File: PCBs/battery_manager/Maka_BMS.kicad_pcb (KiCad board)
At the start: 2 copper layers, 39 x 35.2 mm, 83 parts, among them J8 T1M-10-F-SH-L-K, J9 Molex 087340-1424, Q1 FDC645N, Q2 FDC645N, Q3 FDC645N, Q4 Si3483CDV, Q5 Si3483CDV, Q6 FDC645N, U1 AP63205, U2 TPS70933DBV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

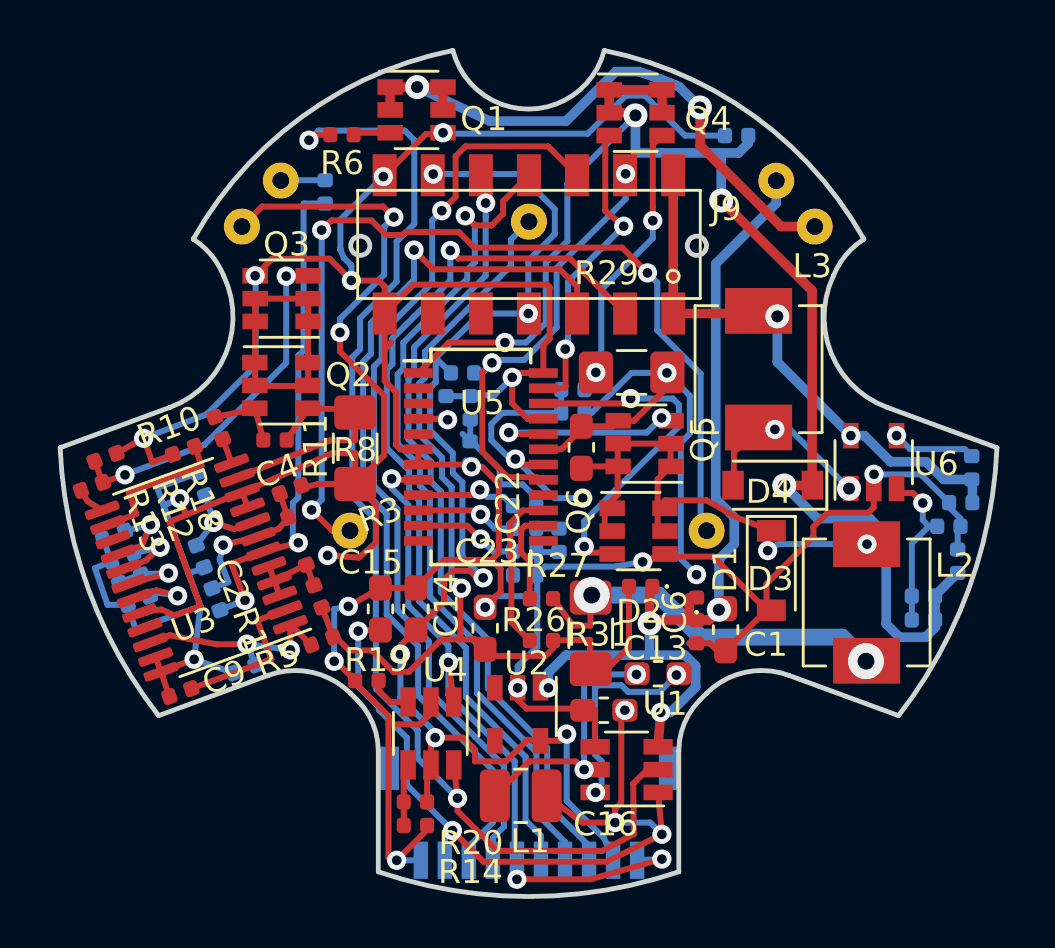
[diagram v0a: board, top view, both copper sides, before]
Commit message: Icreased trace thickness and rerouted higher freq and power paths in the battery management board
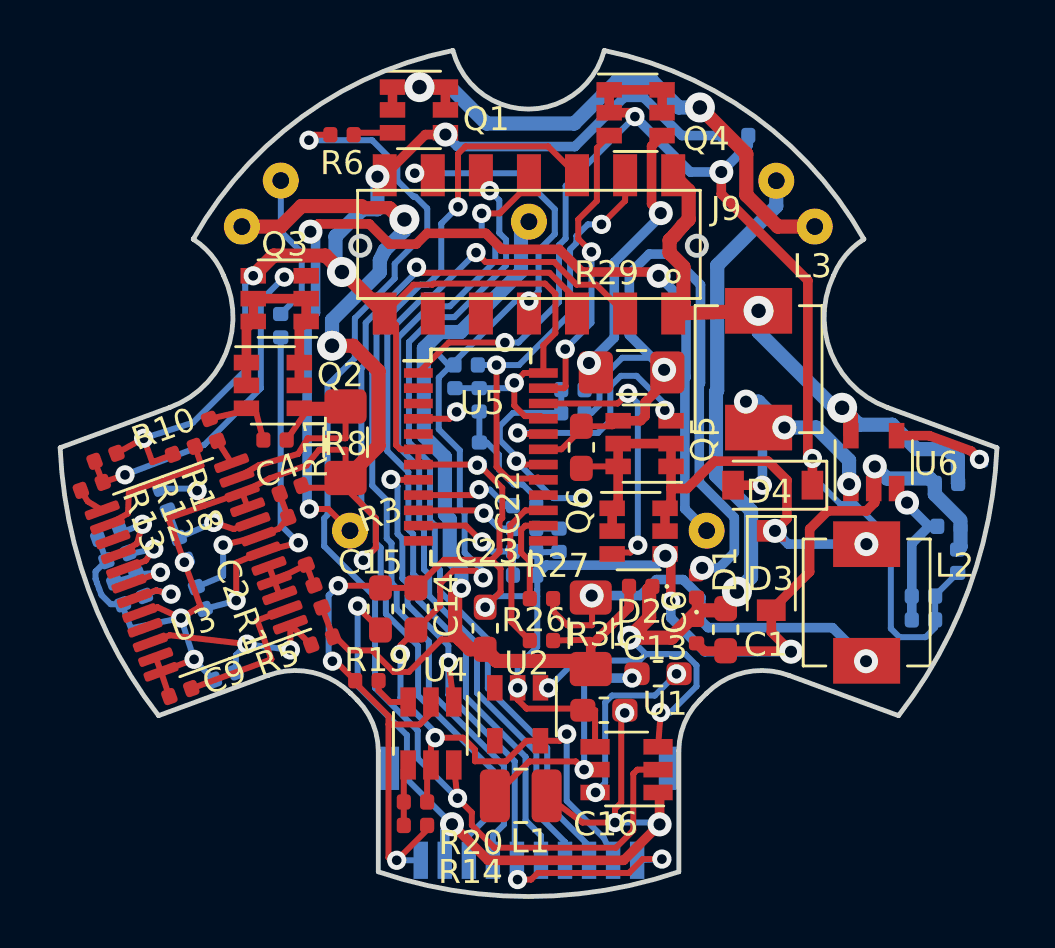
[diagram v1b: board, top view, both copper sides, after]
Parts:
- C24: value 1.75uF -> 0.15uF
- moved R2 5.86 mm to (142.1, 97.4)
- moved C5 1.67 mm to (137.2, 104.6)
- moved C7 1.00 mm to (169.8, 103.9)
- moved C8 0.86 mm to (139.8, 111.9)
- moved R4 0.80 mm to (138.0, 106.7)
- moved C3 0.65 mm to (138.7, 108.7)
- moved R24 0.50 mm to (149.3, 100.5)
- moved TH2 0.50 mm to (150.3, 100.5)
- moved R8 0.47 mm to (144.8, 102.2)
- moved C17 0.39 mm to (150.3, 102.7)
- moved R23 0.36 mm to (149.8, 99.0)
- moved Q2 0.35 mm to (141.8, 99.8)
- moved R21 0.34 mm to (170.7, 103.0), turned to 180 degrees
- moved R10 0.24 mm to (139.3, 101.7)
- moved R16 0.20 mm to (135.3, 107.0)
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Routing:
- net VCC: track 20.2 -> 33.9 mm
- net -BATT: track 69.6 -> 58.8 mm, vias 5 -> 7
- net Net-(C2-Pad1): track 21.0 -> 14.5 mm
- net Net-(7.4-Pad1): track 1.85 -> 6.29 mm
- net Net-(D4-Pad2): track 6.90 -> 11.3 mm, vias 2 -> 4
- net Earth: track 145.4 -> 149.4 mm, vias 14 -> 16
- net Net-(Q6-Pad2): track 14.7 -> 11.3 mm
- net +15V: track 58.7 -> 56.1 mm
- net Net-(12V_OUT1-Pad1): track 37.9 -> 40.5 mm
- net Net-(Q5-Pad2): track 8.07 -> 10.3 mm
- net Net-(Q2-Pad1): track 11.7 -> 9.67 mm
- net +12V: track 22.3 -> 24.0 mm
- net Net-(C22-Pad1): track 21.6 -> 23.2 mm
- net +BATT: track 39.6 -> 41.0 mm
- net Net-(L2-Pad2): track 15.9 -> 17.3 mm
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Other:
- net class 2.2A_Power added: clearance 0.2, trace_width 0.59, via_dia 1.25, via_drill 0.6
- net class 2.5A_Power removed
- board text added: "Maka"
- board text added: "Niu BMS"
- board text added: "rev.0"

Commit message: updates to battery managemennt wayfinder boards, and makaniu hall sensor ring and BMS
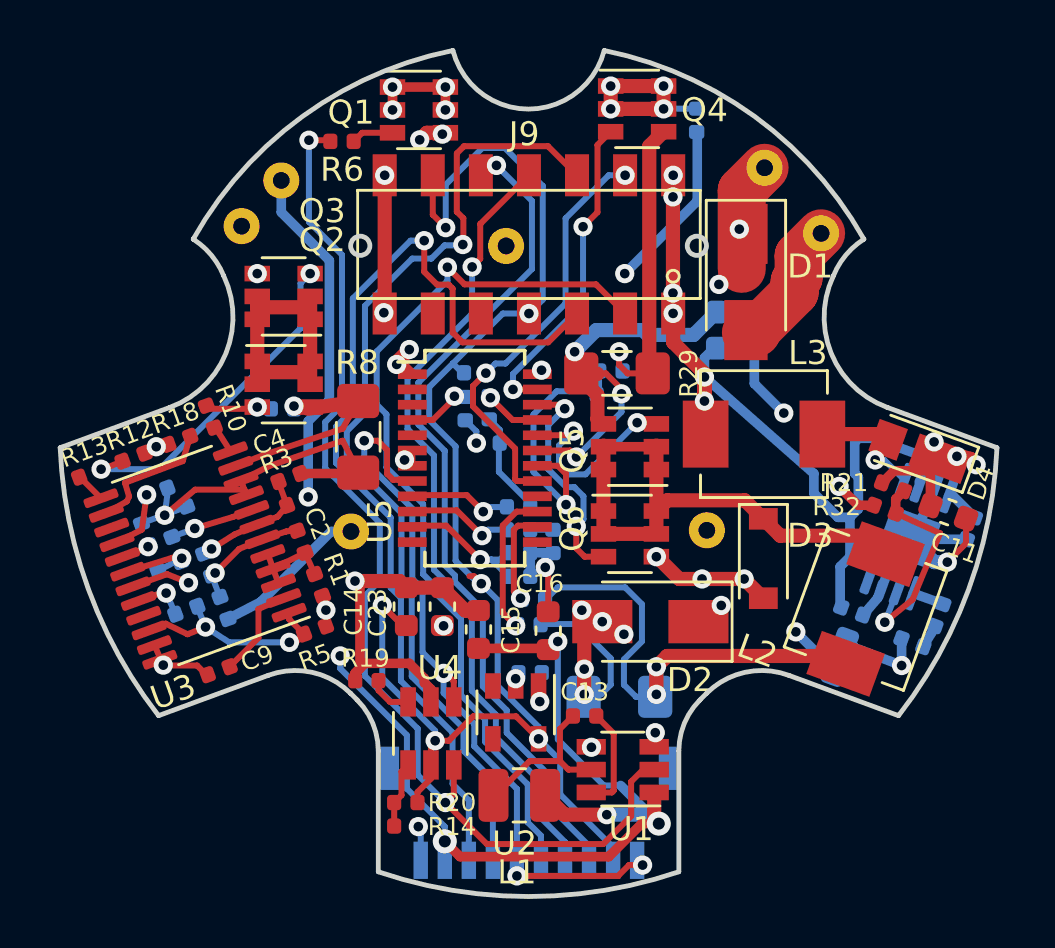
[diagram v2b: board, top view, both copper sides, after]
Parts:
- removed 3.4_2: 3.4+, Custom:TruHole_Batter_Contact_Pad_with_9mm_clear
- removed 7.4: 7.4, TestPoint:TestPoint_THTPad_D1.5mm_Drill0.7mm
- removed C24: 0.15uF, Capacitor_SMD:C_0402_1005Metric
- removed R33: 150K, Resistor_SMD:R_0402_1005Metric
- added 7.4_1: 7.4, Custom:TruHole_Batter_Contact_Pad_with_9mm_clear, B.Cu at (145.0, 105.9)
- added 7.4_2: 7.4, Custom:TruHole_Batter_Contact_Pad_with_9mm_clear, B.Cu at (159.8, 105.9)
- added C11: 10uF, Capacitor_SMD:C_0603_1608Metric, F.Cu at (169.8, 105.1)
- added C12: 15nF, Capacitor_SMD:C_0402_1005Metric, B.Cu at (170.8, 105.8)
- added R7: 100K, Resistor_SMD:R_0402_1005Metric, B.Cu at (165.8, 109.2)
- added R9: 15K, Resistor_SMD:R_0402_1005Metric, B.Cu at (168.3, 110.5)
- 0.0: renamed from 0_1; value 0 -> 0.0; footprint TestPoint:TestPoint_THTPad_D1.5mm_Drill0.7mm -> Custom:TruHole_Batter_Contact_Pad_with_9mm_clear
- 11.1: footprint Custom:TruHole_Batter_Contact_Pad_with_9mm_clear -> TestPoint:TestPoint_THTPad_D1.5mm_Drill0.7mm
- 3.4: renamed from 3.4_1; value 3.4- -> 3.4; footprint Custom:TruHole_Batter_Contact_Pad_with_9mm_clear -> TestPoint:TestPoint_THTPad_D1.5mm_Drill0.7mm
- C1: footprint Capacitor_SMD:C_0603_1608Metric_Pad1.05x0.95mm_HandSolder -> Capacitor_SMD:C_0603_1608Metric; moved to B.Cu
- C10: value 4.7uF -> 1nF
- C13: value 10uF -> 0.1uF; footprint Capacitor_SMD:C_0603_1608Metric_Pad1.05x0.95mm_HandSolder -> Capacitor_SMD:C_0402_1005Metric
- C14, C15, C16: footprint Capacitor_SMD:C_0603_1608Metric_Pad1.05x0.95mm_HandSolder -> Capacitor_SMD:C_0603_1608Metric
- C18: value 0.1Uf -> 0.1uF
- C19: value 0.12uF -> 0.22uF
- C22: value 20uF -> 22uF; footprint Capacitor_SMD:C_0603_1608Metric_Pad1.05x0.95mm_HandSolder -> Capacitor_SMD:C_0603_1608Metric; moved to B.Cu
- C23: value 20uF -> 22uF; footprint Capacitor_SMD:C_0603_1608Metric_Pad1.05x0.95mm_HandSolder -> Capacitor_SMD:C_0603_1608Metric
- C6, R11, R26, R27: moved to B.Cu
- C7: value 2.2uF -> 10uF; footprint Capacitor_SMD:C_0402_1005Metric -> Capacitor_SMD:C_0603_1608Metric
- D1, D2: value BAS5202VH6327 -> 30V 5A; footprint Diode_SMD:D_0402_1005Metric -> Diode_SMD:D_SMA
- D4: value CRS08 -> 30V 3A; footprint Diode_SMD:D_SOD-123 -> Custom:D_SOD-123EP
- R10: value 4.5K -> 10K
- R18: value 450K -> 470K
- R19: value 250K -> 270K
- R21: value 47K -> 110K; moved to F.Cu
- R29: value 0.033 -> 0.06
- R31: value 0.025 -> 0.1; moved to B.Cu
- R32: value 13.3K -> 10K; moved to F.Cu
- R8: value 0.001 -> 0.02
- TH2: value 10K -> DNP
- U6: value LMR62014XMF -> MP3213; footprint Package_TO_SOT_SMD:SOT-23-5 -> Package_SO:MSOP-8-1EP_3x3mm_P0.65mm_EP1.95x2.15mm; moved to B.Cu
- moved 3.4 14.8 mm to (142.1, 91.3)
- moved D1 12.8 mm to (161.4, 95.5), turned to 270 degrees
- moved R2 12.0 mm to (139.7, 109.1), turned to 290 degrees
- moved 11.1 12.0 mm to (140.4, 93.2)
- moved 0.0 11.0 mm to (151.4, 94.0)
- moved C7 10.4 mm to (161.0, 98.3)
- moved C22 8.54 mm to (161.0, 96.8), turned to 180 degrees
- moved C6 7.13 mm to (152.4, 111.8), turned to 0 degrees
- moved D4 6.27 mm to (168.7, 102.6), turned to 160 degrees
- moved C1 4.88 mm to (165.3, 111.1), turned to 250 degrees
- moved C15 4.16 mm to (150.3, 110.0)
- moved C16 4.04 mm to (153.2, 110.0), turned to 270 degrees
- moved C13 3.53 mm to (154.7, 113.6)
- moved U6 3.43 mm to (168.2, 106.1), turned to 70 degrees
- moved R21 3.37 mm to (167.5, 104.1), turned to 340 degrees
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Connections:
- net Net-(12V_OUT1-Pad1) renamed /BATT_OUT
- C10 pad 1: +15V -> Net-(C10-Pad1)
- C10 pad 2: Earth -> Net-(C10-Pad2)
- C20 pad 1: VCC -> Net-(C20-Pad1)
- C22 pad 1: Net-(C22-Pad1) -> Earth
- C22 pad 2: VCC -> Net-(C20-Pad1)
- C7 pad 1: Earth -> +12V
- C7 pad 2: +12V -> Earth
- D1 pad 2: VCC -> /GND_OUT
- D3 pad 1: Net-(C22-Pad1) -> Net-(D3-Pad1)
- GND_OUT1 pad 1: Net-(GND_OUT1-Pad1) -> /GND_OUT
- L2 pad 1: Net-(C22-Pad1) -> Net-(D3-Pad1)
- Q1 pad 1: Net-(GND_OUT1-Pad1) -> /GND_OUT
- Q5 pad 1: Net-(C22-Pad1) -> Net-(D3-Pad1)
- Q5 pad 3: VCC -> Net-(C20-Pad1)
- Q6 pad 1: Net-(C22-Pad1) -> Net-(D3-Pad1)
- R21 pad 1: Net-(R21-Pad1) -> +15V
- R21 pad 2: +12V -> Net-(R21-Pad2)
- R29 pad 1: VCC -> Net-(C20-Pad1)
- R32 pad 1: Net-(C24-Pad1) -> Net-(R21-Pad2)
- U5 pad 19: VCC -> Net-(C20-Pad1)
- U6 pad 1: Net-(D4-Pad2) -> Net-(C10-Pad1)
- U6 pad 2: Earth -> Net-(R21-Pad2)
- U6 pad 3: Net-(C24-Pad1) -> Net-(R7-Pad2)
- U6 pad 4: Net-(R21-Pad1) -> Earth
- U6 pad 5: +12V -> Net-(D4-Pad2)
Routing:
- net Earth: track 149.4 -> 68.5 mm, vias 16 -> 23
- net VCC: track 33.9 -> 0.00 mm, vias 2 -> 0
- net +BATT: track 41.0 -> 10.6 mm, vias 1 -> 7
- net -BATT: track 58.8 -> 30.3 mm, vias 7 -> 3
- net Net-(3.4-Pad1): track 41.2 -> 14.4 mm, vias 3 -> 1
- net Net-(GND_OUT1-Pad1): track 25.4 -> 0.00 mm, vias 2 -> 0
- net +15V: track 56.1 -> 31.5 mm, vias 4 -> 9
- net Net-(C22-Pad1): track 23.2 -> 0.00 mm, vias 2 -> 0
- net Net-(D3-Pad1): track 0.00 -> 22.4 mm
- net Net-(C20-Pad1): track 0.00 -> 17.4 mm, vias 0 -> 3
- net +12V: track 24.0 -> 33.9 mm, vias 2 -> 6
- net /GND_OUT: track 0.00 -> 9.68 mm, vias 0 -> 4
- net Net-(C2-Pad1): track 14.5 -> 5.10 mm, vias 2 -> 1
- net Net-(R21-Pad2): track 0.00 -> 9.11 mm, vias 0 -> 1
- net +3V3: track 51.9 -> 60.5 mm
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- added copper zone on In2.Cu, net +12V
- added copper zone on In2.Cu, net +15V
- added copper zone on In2.Cu, net +BATT
- added copper zone on In1.Cu, net -BATT
- added copper zone on In1.Cu, net /GND_OUT
- added copper zone on In1.Cu, net Earth
- added copper zone on In2.Cu, net Net-(7.4_1-Pad1)
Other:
- copper layers 2 -> 4
- board text added: "rev.1"
- board text removed: "rev.0"

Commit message: updated the repo with all latest pcb changes for the 6cell bms, 3cell bms, and for the wireless charger. Also added sensor data readme filein the same directory as the makaniu python program
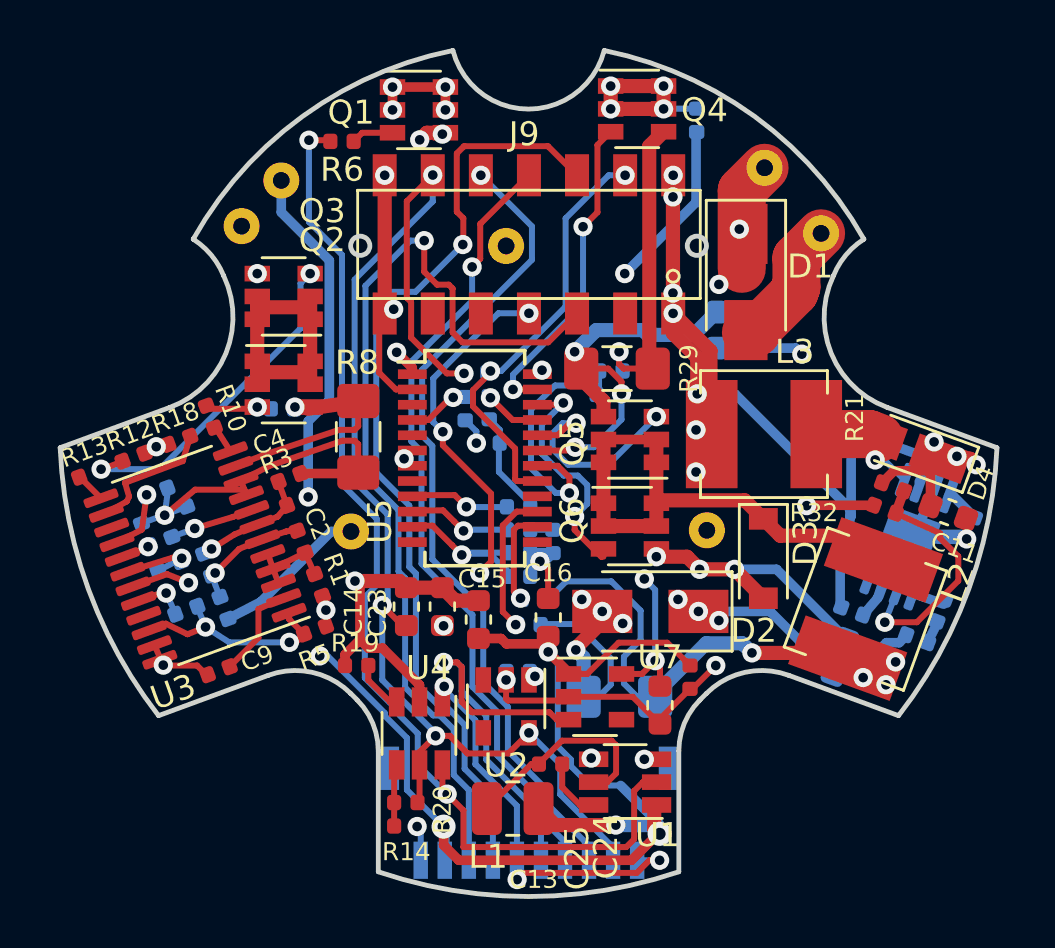
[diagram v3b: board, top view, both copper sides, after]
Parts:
- added C24: 1uF, Capacitor_SMD:C_0402_1005Metric, F.Cu at (159.1, 112.0)
- added C25: 4.7uF, Capacitor_SMD:C_0603_1608Metric, F.Cu at (157.8, 113.2)
- added U7: TPS70933DBV, Package_TO_SOT_SMD:SOT-23-5, F.Cu at (155.2, 112.8)
- C12: value 15nF -> 1uF
- C19: value 0.22uF -> 1uF
- D4: value 30V 3A -> 60V 3A
- J8: value T1M-10-F-SH-L-K -> ‎SAM16035-ND‎
- L2, L3: value 10uH IHLP2020 -> 10uH; footprint Inductor_SMD:L_Vishay_IHLP-2020 -> Custom:MPL-SE6040-100
- R29: value 0.06 -> 0.25
- TH2: value DNP -> 10K
- moved C13 2.45 mm to (153.3, 115.6)
- moved R19 0.76 mm to (145.2, 111.5)
- moved L1 0.61 mm to (151.7, 117.5)
- moved C16 0.55 mm to (153.2, 109.5)
- moved U1 0.53 mm to (156.4, 116.3)
- moved C6 0.50 mm to (151.9, 111.8)
- moved U4 0.47 mm to (147.8, 114.3)
- moved U2 0.47 mm to (151.4, 113.2)
- moved D2 0.42 mm to (157.4, 109.2)
- moved C15 0.41 mm to (150.3, 109.6)
- moved Q6 0.33 mm to (156.6, 105.7)
- moved Q5 0.30 mm to (156.6, 102.1)
- moved R9 0.26 mm to (168.5, 110.4)
- moved C10 0.21 mm to (169.5, 109.2)
- moved R29 0.20 mm to (156.1, 99.2)
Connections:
- J8 pad 06: ~INT~ -> ENDCAP_EN
- J9 pad 3: ~INT~ -> Net-(J9-Pad3)
- J9 pad 7: +3V3 -> +3.3VP
- U5 pad 2: Net-(U5-Pad2) -> Earth
- U5 pad 8: ~SHT_DWN_SIG~ -> Net-(U5-Pad8)
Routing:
- net ~INT~: track 36.9 -> 0.00 mm, vias 1 -> 0
- net +3.3VP: track 0.00 -> 27.7 mm, vias 0 -> 5
- net Earth: track 68.5 -> 86.2 mm
- net ENDCAP_EN: track 0.00 -> 17.3 mm, vias 0 -> 1
- net ~SHT_DWN_SIG~: track 31.4 -> 17.2 mm, vias 4 -> 3
- net +5V: track 39.8 -> 50.5 mm
- net +3V3: track 60.5 -> 52.1 mm, vias 6 -> 5
- net +12V: track 33.9 -> 37.4 mm, vias 6 -> 7
- net Net-(C13-Pad1): track 6.85 -> 8.89 mm
- net Net-(C13-Pad2): track 4.37 -> 2.57 mm
- net Net-(R21-Pad2): track 9.11 -> 10.6 mm
- net Net-(L2-Pad2): track 20.3 -> 18.9 mm, vias 2 -> 4
- net IMU_INT: track 35.2 -> 34.1 mm
- net /BATT_OUT: track 47.9 -> 46.8 mm, vias 6 -> 7
- net SDA: track 40.6 -> 39.5 mm
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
